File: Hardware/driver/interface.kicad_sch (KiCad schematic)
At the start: 58 parts, among them J201 Conn_02x10_Odd_Even, Q201 MMBT3904, Q202 PN2222A, U201 AT24CS32-SSHM, U203 ADUM1250, U204 MCP1804x-C002xMB, U205 FODM217B, U206 EMC2101-R, U207 MCP1703AT-5002E/DB

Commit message: Fixed I2C bus reversal on driver
- Fixed an issue where SCL and SDA for the I2C bus were swapped beyond
  the interface sheet, meaning only the EEPROM is accessible over the
  bus. (This can probably be bodged relatively simply on a rev1 board on
  the bottom where the I2C bus runs)

- Manufacturability tweaks for TDK choke
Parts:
- M201: value (none) -> Fan_4pin; footprint (none) -> programmable-load:Molex-47053-1000-MFG
- U202: value (none) -> MIC5366-3.3YC5; footprint (none) -> Package_TO_SOT_SMD:SOT-353_SC-70-5
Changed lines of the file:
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@@
       (effects (font (size 1.27 1.27)) hide)
     )
-    (property "Value" "" (id 1) (at 230.505 113.03 90)
+    (property "Value" "+12VA" (id 1) (at 230.505 113.03 90)
       (effects (font (size 1.27 1.27)) (justify left))
     )
@@
     (in_bom yes) (on_board yes) (fields_autoplaced)
     (property "Reference" "U202" (id 0) (at 68.58 72.39 0))
-    (property "Value" "" (id 1) (at 68.58 74.93 0))
-    (property "Footprint" "" (id 2) (at 68.58 73.66 0)
+    (property "Value" "MIC5366-3.3YC5" (id 1) (at 68.58 74.93 0))
+    (property "Footprint" "Package_TO_SOT_SMD:SOT-353_SC-70-5" (id 2) (at 68.58 73.66 0)
       (effects (font (size 1.27 1.27)) hide)
     )
@@
       (effects (font (size 1.27 1.27)) (justify left))
     )
-    (property "Value" "" (id 1) (at 273.05 111.7599 0)
-      (effects (font (size 1.27 1.27)) (justify left))
-    )
-    (property "Footprint" "" (id 2) (at 268.605 110.236 0)
-      (effects (font (size 1.27 1.27)) hide)
-    )
+    (property "Value" "Fan_4pin" (id 1) (at 273.05 111.7599 0)
+      (effects (font (size 1.27 1.27)) (justify left))
+    )
+    (property "Footprint" "programmable-load:Molex-47053-1000-MFG" (id 2) (at 268.605 110.236 0)
+      (effects (font (size 1.27 1.27)) hide)
+    )

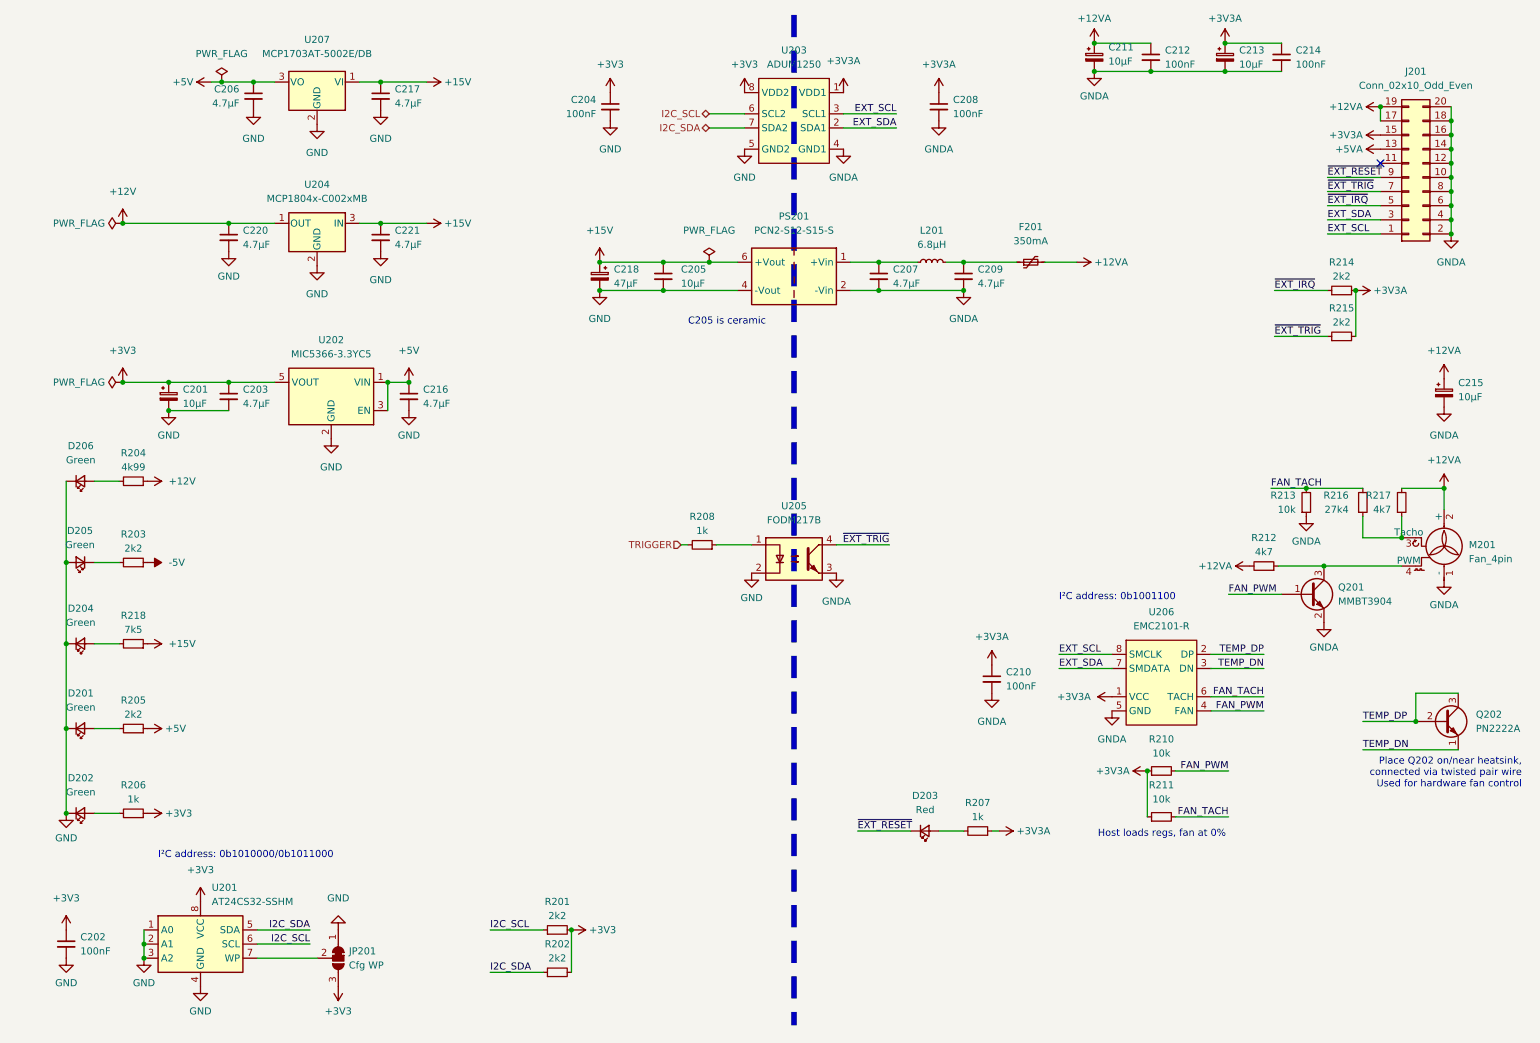
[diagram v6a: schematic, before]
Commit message: Final bits of tweaks for rev2 analog board
- Fixed footprint of MMBT3904 transistors on driver and controller
  boards (it is SOT-323, not SC-70)

- A few more minor modifications to the layout of the analog driver
  board for rev2
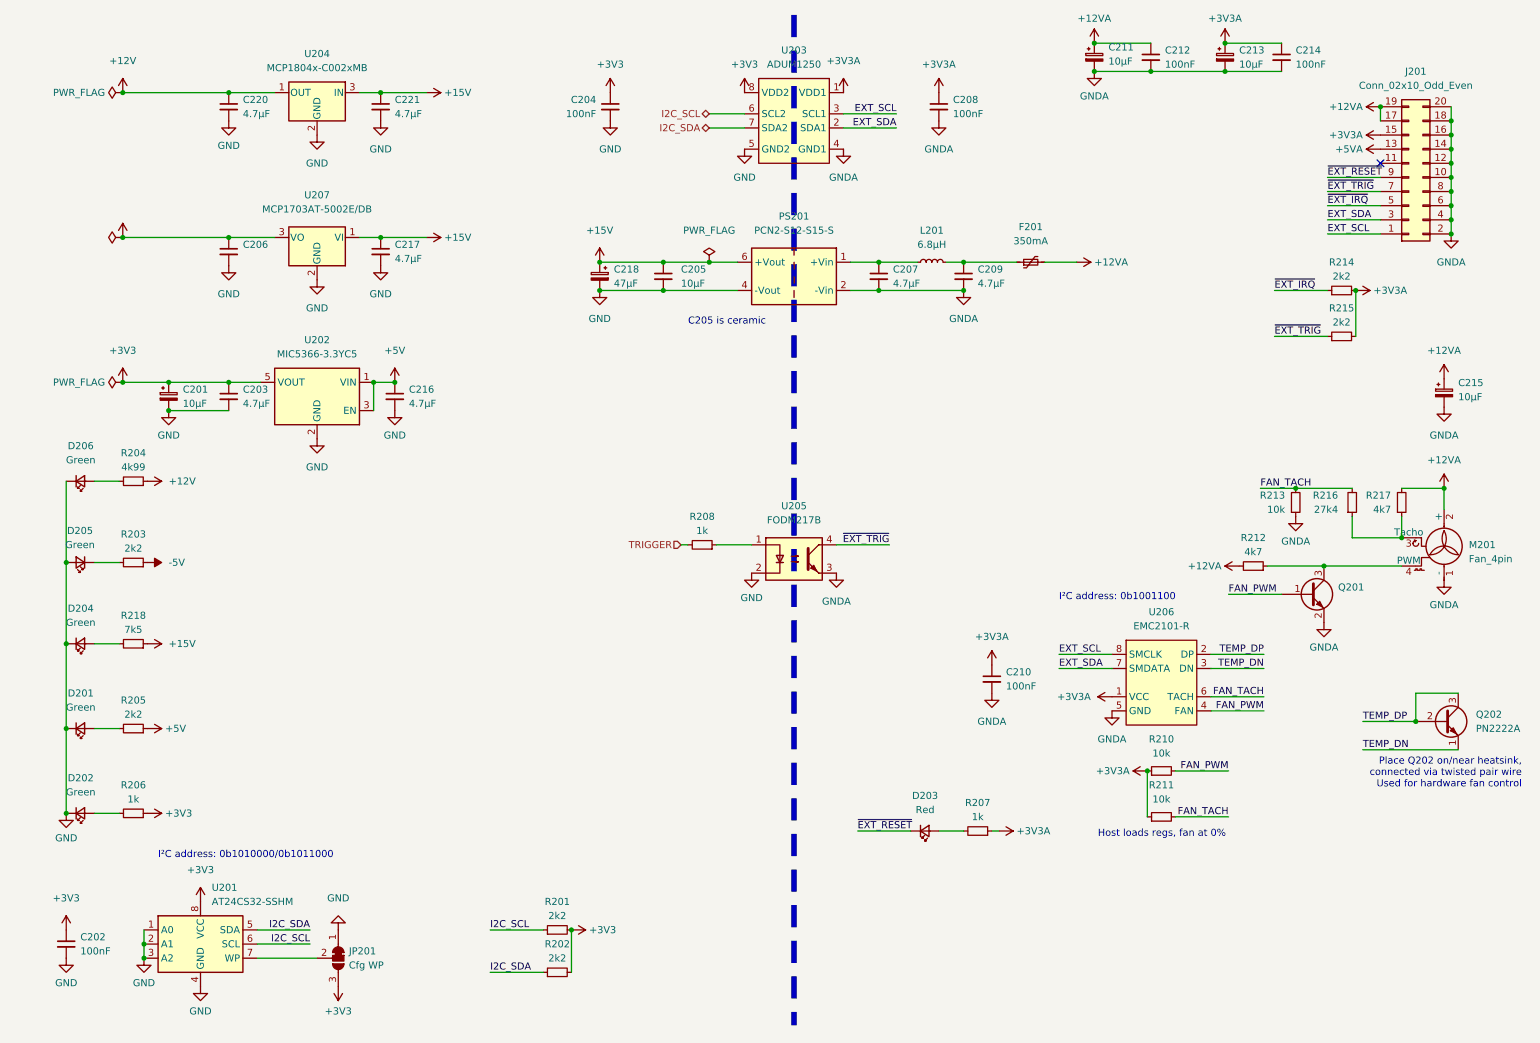
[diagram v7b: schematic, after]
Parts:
- C206: value 4.7µF -> (none); footprint Capacitor_SMD:C_0805_2012Metric_Pad1.18x1.45mm_HandSolder -> (none)
- Q201: value MMBT3904 -> (none); footprint Package_TO_SOT_SMD:SOT-23 -> (none)
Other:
- moved on the sheet: C206, C216, C217, C220, C221, R212, R213, R216, U202, U204, U207

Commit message: Fixed a few more footprints
- Made heatsink and connector mechanical/mounting pads NPTH instead of
  normal pads, so they're not tempted to be connected to regular signals
  on the board and get more keepout space
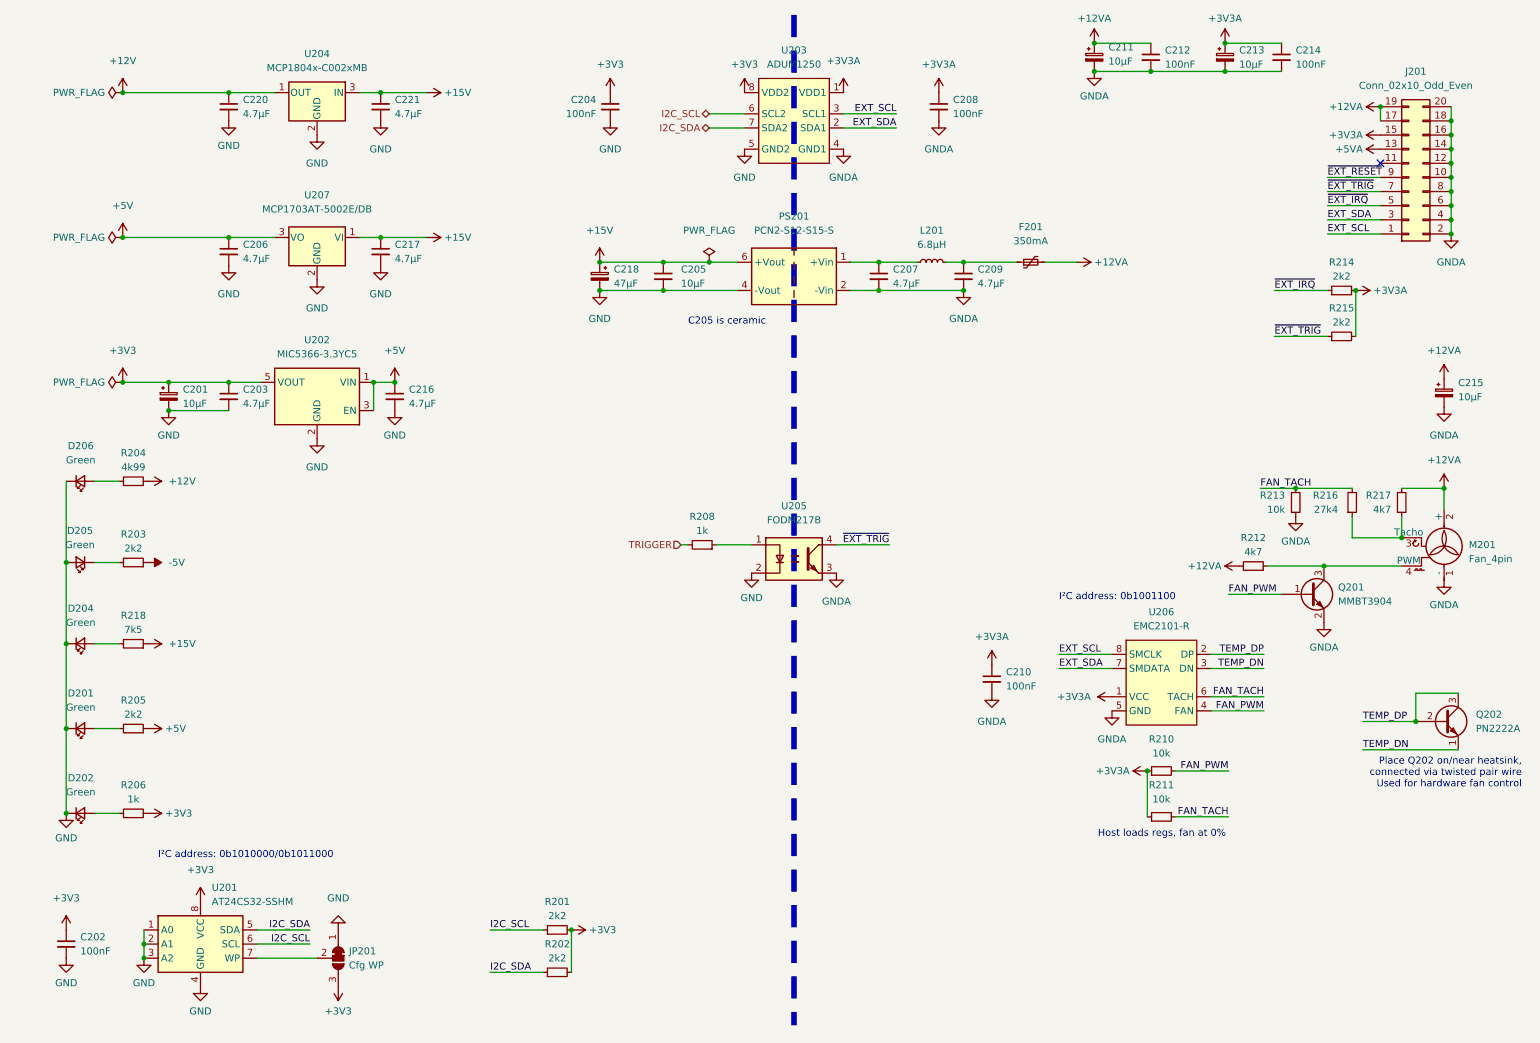
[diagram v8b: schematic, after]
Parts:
- removed D203: Red, LED_SMD:LED_0805_2012Metric_Pad1.15x1.40mm_HandSolder, symbol Device:LED_Small
- removed R207: 1k, Resistor_SMD:R_0805_2012Metric_Pad1.20x1.40mm_HandSolder, symbol Device:R_Small
- C206: value (none) -> 4.7µF; footprint (none) -> Capacitor_SMD:C_0805_2012Metric_Pad1.18x1.45mm_HandSolder
- Q201: value (none) -> MMBT3904; footprint (none) -> Package_TO_SOT_SMD:SOT-323_SC-70_Handsoldering
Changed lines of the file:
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@@
-    (stroke (width 0) (type default) (color 0 0 0 0))
-  )
-  (wire (pts (xy 187.325 160.655) (xy 188.595 160.655))
     (stroke (width 0) (type default) (color 0 0 0 0))
   )
@@
   )
   (wire (pts (xy 269.875 48.26) (xy 269.875 50.8))
-    (stroke (width 0) (type default) (color 0 0 0 0))
-  )
-  (wire (pts (xy 177.8 160.655) (xy 182.245 160.655))
     (stroke (width 0) (type default) (color 0 0 0 0))
   )
@@
   (polyline (pts (xy 151.765 13.97) (xy 151.765 195.58))
     (stroke (width 1) (type dash) (color 0 0 0 0))
-  )
-  (wire (pts (xy 163.195 160.655) (xy 172.72 160.655))
-    (stroke (width 0) (type default) (color 0 0 0 0))
   )
   (wire (pts (xy 116.84 63.5) (xy 128.27 63.5))
@@
   )
   (label "FAN_TACH" (at 235.585 99.06 0)
-    (effects (font (size 1.27 1.27)) (justify left bottom))
-  )
-  (label "~{EXT_RESET}" (at 163.195 160.655 0)
     (effects (font (size 1.27 1.27)) (justify left bottom))
   )
@@
     (pin "1")
   )
-  (symbol (lib_id "Device:R_Small") (at 184.785 160.655 270) (mirror x) (unit 1)
-    (in_bom yes) (on_board yes)
-    (property "Reference" "R207" (id 0) (at 184.785 155.575 90))
-    (property "Value" "1k" (id 1) (at 184.785 158.115 90))
-    (property "Footprint" "Resistor_SMD:R_0805_2012Metric_Pad1.20x1.40mm_HandSolder" (id 2) (at 184.785 160.655 0)
-      (effects (font (size 1.27 1.27)) hide)
-    )
-    (property "Datasheet" "~" (id 3) (at 184.785 160.655 0)
-      (effects (font (size 1.27 1.27)) hide)
-    )
-    (property "MPN" "CR0805-JW-102ELF" (id 4) (at 184.785 160.655 90)
-      (effects (font (size 1.27 1.27)) hide)
-    )
-    (pin "1")
-    (pin "2")
-  )
   (symbol (lib_id "power:PWR_FLAG") (at 31.115 80.01 90) (unit 1)
     (in_bom yes) (on_board yes)
@@
       (effects (font (size 1.27 1.27)) hide)
     )
-    (property "Value" "" (id 1) (at 31.115 48.26 0))
+    (property "Value" "+5V" (id 1) (at 31.115 48.26 0))
     (property "Footprint" "" (id 2) (at 31.115 53.975 0)
       (effects (font (size 1.27 1.27)) hide)
@@
       (effects (font (size 1.27 1.27)) (justify left))
     )
-    (property "Value" "" (id 1) (at 249.555 119.3799 0)
-      (effects (font (size 1.27 1.27)) (justify left))
-    )
-    (property "Footprint" "" (id 2) (at 249.555 120.015 0)
+    (property "Value" "MMBT3904" (id 1) (at 249.555 119.3799 0)
+      (effects (font (size 1.27 1.27)) (justify left))
+    )
+    (property "Footprint" "Package_TO_SOT_SMD:SOT-323_SC-70_Handsoldering" (id 2) (at 249.555 120.015 0)
       (effects (font (size 1.27 1.27) italic) (justify left) hide)
     )
@@
       (effects (font (size 1.27 1.27)) (justify left))
     )
-    (property "Value" "" (id 1) (at 52.705 57.7912 0)
-      (effects (font (size 1.27 1.27)) (justify left))
-    )
-    (property "Footprint" "" (id 2) (at 50.165 56.515 0)
+    (property "Value" "4.7µF" (id 1) (at 52.705 57.7912 0)
+      (effects (font (size 1.27 1.27)) (justify left))
+    )
+    (property "Footprint" "Capacitor_SMD:C_0805_2012Metric_Pad1.18x1.45mm_HandSolder" (id 2) (at 50.165 56.515 0)
       (effects (font (size 1.27 1.27)) hide)
     )
@@
     )
     (pin "1")
-  )
-  (symbol (lib_id "Device:LED_Small") (at 175.26 160.655 0) (mirror x) (unit 1)
-    (in_bom yes) (on_board yes) (fields_autoplaced)
-    (property "Reference" "D203" (id 0) (at 175.3235 154.305 0))
-    (property "Value" "Red" (id 1) (at 175.3235 156.845 0))
-    (property "Footprint" "LED_SMD:LED_0805_2012Metric_Pad1.15x1.40mm_HandSolder" (id 2) (at 175.26 160.655 90)
-      (effects (font (size 1.27 1.27)) hide)
-    )
-    (property "Datasheet" "~" (id 3) (at 175.26 160.655 90)
-      (effects (font (size 1.27 1.27)) hide)
-    )
-    (property "MPN" "150080SS75000" (id 4) (at 175.26 160.655 0)
-      (effects (font (size 1.27 1.27)) hide)
-    )
-    (pin "1")
-    (pin "2")
   )
   (symbol (lib_id "power:PWR_FLAG") (at 31.115 27.94 90) (unit 1)
@@
       (effects (font (size 1.27 1.27)) hide)
     )
-    (property "Value" "" (id 1) (at 27.94 53.9749 90)
+    (property "Value" "PWR_FLAG" (id 1) (at 27.94 53.9749 90)
       (effects (font (size 1.27 1.27)) (justify left))
     )
@@
       (effects (font (size 1.27 1.27)) hide)
     )
-    (pin "1")
-  )
-  (symbol (lib_id "programmable-load:+3V3A") (at 188.595 160.655 270) (unit 1)
-    (in_bom yes) (on_board yes) (fields_autoplaced)
-    (property "Reference" "#PWR0127" (id 0) (at 184.785 160.655 0)
-      (effects (font (size 1.27 1.27)) hide)
-    )
-    (property "Value" "+3V3A" (id 1) (at 191.77 160.6549 90)
-      (effects (font (size 1.27 1.27)) (justify left))
-    )
-    (property "Footprint" "" (id 2) (at 188.595 160.655 0)
-      (effects (font (size 1.27 1.27)) hide)
-    )
-    (property "Datasheet" "" (id 3) (at 188.595 160.655 0)
-      (effects (font (size 1.27 1.27)) hide)
-    )
